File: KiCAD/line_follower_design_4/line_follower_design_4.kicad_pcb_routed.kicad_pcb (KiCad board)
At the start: 2 copper layers, 50 parts, among them M1 Motor Levi, M2 Motor Desni, Q1 Q_NPN_BCE, Q2 BSS138, Q3 BSS138, Q4 Q_PMOS_GDS, SW1 switch_psh, SW2 switch, U1 MCP1703A-5002/MB

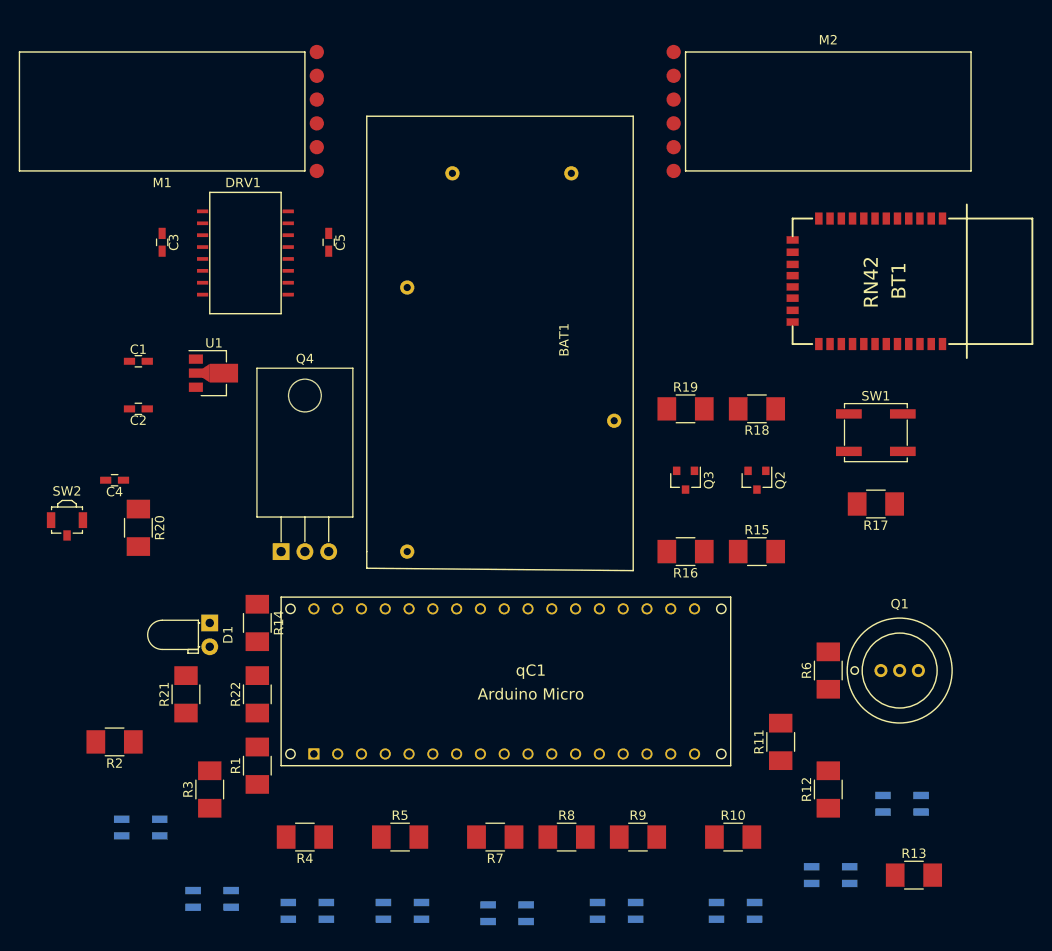
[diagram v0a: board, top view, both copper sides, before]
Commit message: line-follower-design-4 PCB and Routing
PCB and routing files for design. no. 4. First finished iteration. Some
clearance issues.
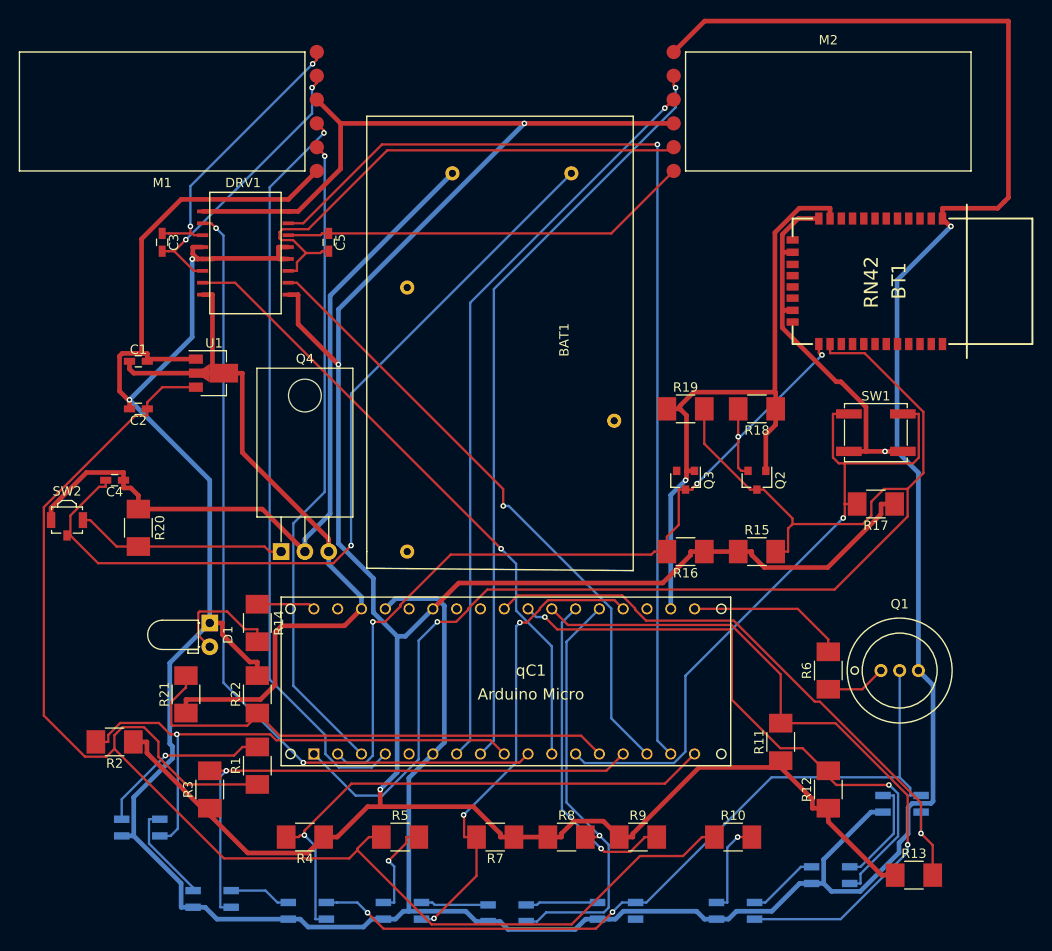
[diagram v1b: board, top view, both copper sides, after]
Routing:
- net GND: track 0.00 -> 472.3 mm, vias 0 -> 4
- net +5V: track 0.00 -> 320.0 mm, vias 0 -> 3
- net Net-(C2-Pad1): track 0.00 -> 154.5 mm
- net /BTRX: track 0.00 -> 146.7 mm, vias 0 -> 1
- net /PWMR2: track 0.00 -> 108.6 mm, vias 0 -> 1
- net /BTTX: track 0.00 -> 91.0 mm, vias 0 -> 4
- net Net-(BAT1-Pad2): track 0.00 -> 89.7 mm, vias 0 -> 1
- net /PWML1: track 0.00 -> 87.0 mm, vias 0 -> 2
- net Net-(Q1-Pad2): track 0.00 -> 84.0 mm, vias 0 -> 2
- net +9VA: track 0.00 -> 82.2 mm
- net /ENCRB: track 0.00 -> 81.1 mm, vias 0 -> 1
- net +9V: track 0.00 -> 80.4 mm
- net /ENCLB: track 0.00 -> 80.1 mm, vias 0 -> 1
- net /ENCRA: track 0.00 -> 79.5 mm, vias 0 -> 1
- net /LS7: track 0.00 -> 74.7 mm, vias 0 -> 1
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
